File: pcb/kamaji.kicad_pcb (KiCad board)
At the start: 2 copper layers, 130 x 110 mm, 35 parts, among them J1 RJ10, J2 RJ10, J3 RJ10, J4 RJ10, J5 RJ10, Q1 TIP120, Q2 TIP120, SW1 CTRL1, SW2 CTRL2, SW3 CTRL3, U1 ATMEGA328P-PU

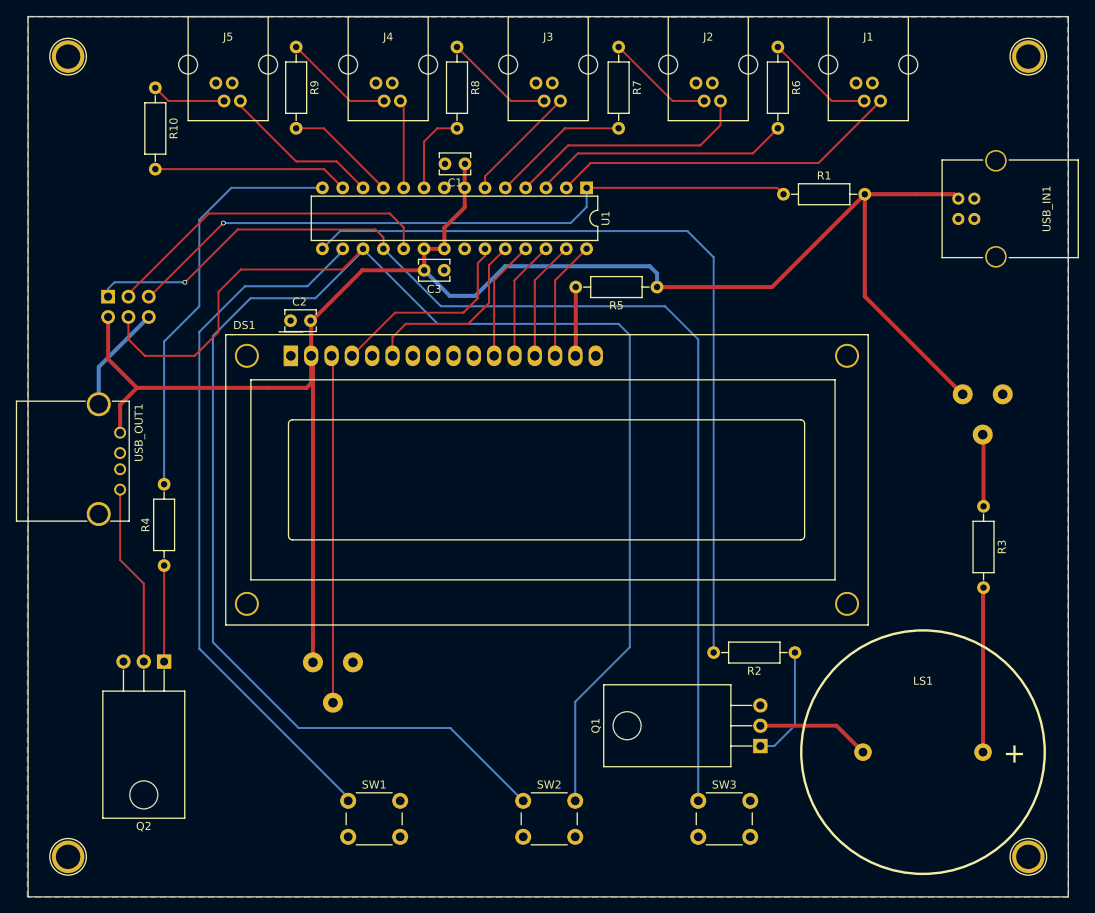
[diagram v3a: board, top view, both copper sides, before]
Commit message: change mounting hole sizes, move labels around
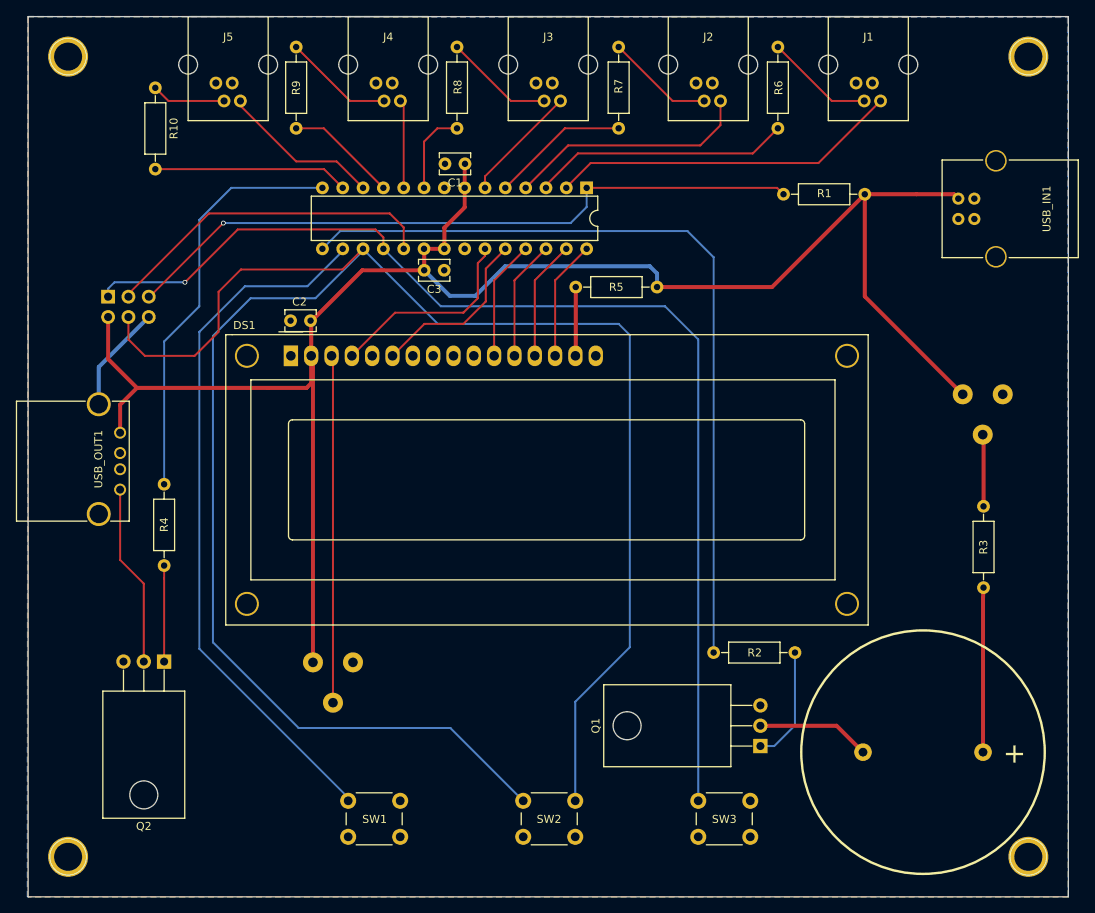
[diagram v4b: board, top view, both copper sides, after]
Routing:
- net LCD_EN: track 23.8 -> 22.1 mm
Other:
- board text added: "Ilya Strukov <iley@iley.ru>"

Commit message: miscellaneous PCB changes
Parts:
- moved USB_OUT1 2.08 mm to (113.2, 83.2)
- moved USB_IN1 1.55 mm to (214.8, 52.2)
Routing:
- net GND: track 13.7 -> 0.23 mm
- net VCC: track 225.6 -> 221.2 mm
- net Net-(Q2-Pad2): track 22.7 -> 20.8 mm
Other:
- rule trace_min: 0.2 -> 0.25
- board text added: "CONTRAST"
- board text added: "Kamaji 1.0"
- board text added: "VOLUME"
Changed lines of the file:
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@@
     (area 99.924999 29.924999 230.075001 140.075001)
     (thickness 1.6)
-    (drawings 5)
-    (tracks 192)
+    (drawings 8)
+    (tracks 185)
     (zones 0)
     (modules 35)
@@
     (zone_clearance 0.508)
     (zone_45_only no)
-    (trace_min 0.2)
+    (trace_min 0.25)
     (segment_width 0.2)
     (edge_width 0.15)
@@
     (descr "C, Disc series, Radial, pin pitch=2.50mm, , diameter*width=3.8*2.6mm^2, Capacitor, http://www.vishay.com/docs/45233/krseries.pdf")
     (tags "C Disc series Radial pin pitch 2.50mm  diameter 3.8mm width 2.6mm Capacitor")
-    (fp_text reference C1 (at 1.25 -2.36 180) (layer F.SilkS)
+    (fp_text reference C1 (at 4.3 -0.2 180) (layer F.SilkS)
       (effects (font (size 1 1) (thickness 0.15)))
     )
@@
     (descr "LCD 16x2 http://www.wincomlcd.com/pdf/WC1602A-SFYLYHTC06.pdf")
     (tags "LCD 16x2 Alphanumeric 16pin")
-    (fp_text reference DS1 (at -5.82 -3.81) (layer F.SilkS)
+    (fp_text reference DS1 (at -5.82 -3.81) (layer F.SilkS) hide
       (effects (font (size 1 1) (thickness 0.15)))
     )
@@
     (descr "Resistor, Axial_DIN0207 series, Axial, Horizontal, pin pitch=10.16mm, 0.25W = 1/4W, length*diameter=6.3*2.5mm^2, http://cdn-reichelt.de/documents/datenblatt/B400/1_4W%23YAG.pdf")
     (tags "Resistor Axial_DIN0207 series Axial Horizontal pin pitch 10.16mm 0.25W = 1/4W length 6.3mm diameter 2.5mm")
-    (fp_text reference R10 (at 5.08 -2.31 270) (layer F.SilkS)
+    (fp_text reference R10 (at 4.8 0 270) (layer F.SilkS)
       (effects (font (size 1 1) (thickness 0.15)))
     )
@@
     (descr "Potentiometer, Trimmer, RM-065")
     (tags "Potentiometer Trimmer RM-065")
-    (fp_text reference RV1 (at -2.1 2.5 270) (layer B.SilkS)
+    (fp_text reference RV1 (at 2.4 2 270) (layer B.SilkS)
       (effects (font (size 1 1) (thickness 0.15)) (justify mirror))
     )
@@
     (descr "Potentiometer, Trimmer, RM-065")
     (tags "Potentiometer Trimmer RM-065")
-    (fp_text reference RV2 (at 2.4 2 270) (layer B.SilkS)
+    (fp_text reference RV2 (at 2.4 2.3) (layer B.SilkS)
       (effects (font (size 1 1) (thickness 0.15)) (justify mirror))
     )
@@
   )
   (module Connectors:USB_B (layer F.Cu)
-    (at 216.25 52.75)
+    (at 214.8 52.2)
     (descr "USB B connector")
     (tags "USB_B USB_DEV")
@@
   )
   (module Connectors:USB_A (layer F.Cu)
-    (at 111.5 82 270)
+    (at 113.2 83.2 270)
     (descr "USB A connector")
     (tags "USB USB_A")
@@
       (effects (font (size 1 1) (thickness 0.15)) (justify mirror))
     )
-    (fp_text value ICSP (at 3 -5) (layer B.Fab)
+    (fp_text value ICSP (at 3 -5) (layer B.SilkS)
       (effects (font (size 1 1) (thickness 0.15)) (justify mirror))
     )
@@
     (pad 1 thru_hole circle (at 0 0) (size 5 5) (drill 3.5) (layers *.Cu *.Mask))
   )
-  (gr_text "Ilya Strukov <iley@iley.ru>" (at 104.8 113.1 90) (layer F.Mask)
+  (gr_text VOLUME (at 219.4 85.5) (layer B.SilkS)
+    (effects (font (size 1 1) (thickness 0.15)) (justify mirror))
+  )
+  (gr_text CONTRAST (at 138.2 119.1) (layer B.SilkS)
+    (effects (font (size 1 1) (thickness 0.15)) (justify mirror))
+  )
+  (gr_text "Kamaji 1.0" (at 105 112.7 90) (layer F.SilkS)
+    (effects (font (size 1.5 1.5) (thickness 0.3)))
+  )
+  (gr_text "Ilya Strukov <iley@iley.ru>" (at 105 56.9 90) (layer F.SilkS)
     (effects (font (size 1.5 1.5) (thickness 0.3)))
   )
@@
   (gr_line (start 100 140) (end 100 30) (angle 90) (layer Edge.Cuts) (width 0.15))
   (gr_line (start 230 140) (end 100 140) (angle 90) (layer Edge.Cuts) (width 0.15))
+  (segment (start 113.2 83.2) (end 135.6 83.2) (width 0.5) (layer F.Cu) (net 1) (status 400000))
+  (segment (start 135.6 83.2) (end 135.6 83.1) (width 0.5) (layer F.Cu) (net 1))
+  (segment (start 113.2 83.2) (end 113.2 77.1) (width 0.5) (layer F.Cu) (net 1) (status 400000))
+  (segment (start 110 73.9) (end 110 67.54) (width 0.5) (layer F.Cu) (net 1) (status 800000))
+  (segment (start 113.2 77.1) (end 110 73.9) (width 0.5) (layer F.Cu) (net 1))
+  (segment (start 204.56 52.2) (end 214.8 52.2) (width 0.5) (layer F.Cu) (net 1))
   (segment (start 178.6 63.8) (end 178.6 62.1) (width 0.5) (layer B.Cu) (net 1))
   (segment (start 152.7 64.9) (end 149.5 61.7) (width 0.5) (layer B.Cu) (net 1))
@@
   (segment (start 177.7 61.2) (end 159.6 61.2) (width 0.5) (layer B.Cu) (net 1))
   (segment (start 178.6 62.1) (end 177.7 61.2) (width 0.5) (layer B.Cu) (net 1))
-  (segment (start 135.6 110.7) (end 135.6 72.608) (width 0.5) (layer F.Cu) (net 1))
+  (segment (start 135.6 110.7) (end 135.6 83.1) (width 0.5) (layer F.Cu) (net 1))
+  (segment (start 135.6 83.1) (end 135.6 72.608) (width 0.5) (layer F.Cu) (net 1))
   (segment (start 135.6 72.608) (end 135.382 72.39) (width 0.5) (layer F.Cu) (net 1))
   (segment (start 178.6 63.8) (end 192.96 63.8) (width 0.5) (layer F.Cu) (net 1))
@@
   (segment (start 154.56 48.44) (end 154.6 48.4) (width 0.5) (layer F.Cu) (net 1))
   (segment (start 151.9 59.14) (end 152.02 59.02) (width 0.5) (layer F.Cu) (net 1))
-  (segment (start 204.56 52.2) (end 211 52.2) (width 0.5) (layer F.Cu) (net 1))
-  (segment (start 211 52.2) (end 215.7 52.2) (width 0.5) (layer F.Cu) (net 1))
-  (segment (start 215.7 52.2) (end 216.25 52.75) (width 0.5) (layer F.Cu) (net 1) (status 20))
-  (segment (start 111.5 82) (end 111.5 78.5) (width 0.5) (layer F.Cu) (net 1))
-  (segment (start 111.5 78.5) (end 113.6 76.4) (width 0.5) (layer F.Cu) (net 1))
   (segment (start 149.48 59.02) (end 152.02 59.02) (width 0.5) (layer F.Cu) (net 1) (status 30))
-  (segment (start 110 67.54) (end 110 72.8) (width 0.5) (layer F.Cu) (net 1))
-  (segment (start 135.382 75.818) (end 135.382 72.39) (width 0.5) (layer F.Cu) (net 1))
-  (segment (start 134.8 76.4) (end 135.382 75.818) (width 0.5) (layer F.Cu) (net 1))
-  (segment (start 113.6 76.4) (end 130 76.4) (width 0.5) (layer F.Cu) (net 1))
-  (segment (start 130 76.4) (end 134.8 76.4) (width 0.5) (layer F.Cu) (net 1))
-  (segment (start 110 72.8) (end 113.6 76.4) (width 0.5) (layer F.Cu) (net 1))
   (segment (start 154.61 48.41) (end 154.6 48.4) (width 0.5) (layer F.Cu) (net 1) (status 30))
-  (segment (start 108.83 78.44) (end 108.83 73.79) (width 0.5) (layer B.Cu) (net 2))
-  (segment (start 108.83 73.79) (end 115.08 67.54) (width 0.5) (layer B.Cu) (net 2))
   (segment (start 154.4 59.18) (end 154.56 59.02) (width 0.5) (layer F.Cu) (net 2))
   (segment (start 138.1 115.74) (end 138.1 72.568) (width 0.25) (layer F.Cu) (net 3))
@@
   (segment (start 154.4 67) (end 145.852 67) (width 0.25) (layer F.Cu) (net 4))
   (segment (start 145.852 67) (end 140.462 72.39) (width 0.25) (layer F.Cu) (net 4))
-  (segment (start 159.64 59.02) (end 159.64 59.06) (width 0.25) (layer F.Cu) (net 5) (status C00000))
-  (segment (start 159.64 59.06) (end 157.2 61.5) (width 0.25) (layer F.Cu) (net 5) (status 400000))
+  (segment (start 159.64 59.02) (end 159.64 59.06) (width 0.25) (layer F.Cu) (net 5))
+  (segment (start 159.64 59.06) (end 157.2 61.5) (width 0.25) (layer F.Cu) (net 5))
   (segment (start 157.2 61.5) (end 157.2 65.6) (width 0.25) (layer F.Cu) (net 5))
   (segment (start 157.2 65.6) (end 154.4 68.4) (width 0.25) (layer F.Cu) (net 5))
   (segment (start 154.4 68.4) (end 149.532 68.4) (width 0.25) (layer F.Cu) (net 5))
-  (segment (start 149.532 68.4) (end 145.542 72.39) (width 0.25) (layer F.Cu) (net 5) (status 800000))
+  (segment (start 149.532 68.4) (end 145.542 72.39) (width 0.25) (layer F.Cu) (net 5))
   (segment (start 158.242 72.39) (end 158.242 62.958) (width 0.25) (layer F.Cu) (net 10))
   (segment (start 158.242 62.958) (end 162.18 59.02) (width 0.25) (layer F.Cu) (net 10))
@@
   (segment (start 117 110.6) (end 117 100.2) (width 0.25) (layer F.Cu) (net 29))
   (segment (start 117 100.2) (end 117 98.6) (width 0.25) (layer F.Cu) (net 29) (status 20))
-  (segment (start 111.5 89.11) (end 111.5 97.9) (width 0.25) (layer F.Cu) (net 30))
-  (segment (start 111.5 97.9) (end 114.46 100.86) (width 0.25) (layer F.Cu) (net 30))
-  (segment (start 114.46 100.86) (end 114.46 110.6) (width 0.25) (layer F.Cu) (net 30))
+  (segment (start 114.46 110.6) (end 114.46 91.57) (width 0.25) (layer F.Cu) (net 30) (status 400000))
+  (segment (start 114.46 91.57) (end 113.2 90.31) (width 0.25) (layer F.Cu) (net 30) (status 800000))
   (segment (start 185.674 109.474) (end 185.674 60.074) (width 0.25) (layer B.Cu) (net 31))
   (segment (start 185.674 60.074) (end 182.4 56.8) (width 0.25) (layer B.Cu) (net 31))

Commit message: final touches to the PCB design
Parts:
- moved R1 19.9 mm to (174.5, 51.4)
- moved USB_IN1 0.92 mm to (214.6, 51.3)
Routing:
- net RST: track 86.8 -> 66.5 mm
- net VCC: track 221.2 -> 224.5 mm
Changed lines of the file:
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@@
     (links 87)
     (no_connects 2)
-    (area 99.924999 29.924999 230.075001 140.075001)
+    (area 99.774999 29.55 230.275001 140.075001)
     (thickness 1.6)
     (drawings 8)
-    (tracks 185)
+    (tracks 187)
     (zones 0)
     (modules 35)
@@
   )
   (module Resistors_THT:R_Axial_DIN0207_L6.3mm_D2.5mm_P10.16mm_Horizontal (layer F.Cu)
-    (at 194.4 52.2)
+    (at 174.5 51.4)
     (descr "Resistor, Axial_DIN0207 series, Axial, Horizontal, pin pitch=10.16mm, 0.25W = 1/4W, length*diameter=6.3*2.5mm^2, http://cdn-reichelt.de/documents/datenblatt/B400/1_4W%23YAG.pdf")
     (tags "Resistor Axial_DIN0207 series Axial Horizontal pin pitch 10.16mm 0.25W = 1/4W length 6.3mm diameter 2.5mm")
@@
   )
   (module Connectors:USB_B (layer F.Cu)
-    (at 214.8 52.2)
+    (at 214.6 51.3)
     (descr "USB B connector")
     (tags "USB_B USB_DEV")
@@
   (gr_line (start 100 140) (end 100 30) (angle 90) (layer Edge.Cuts) (width 0.15))
   (gr_line (start 230 140) (end 100 140) (angle 90) (layer Edge.Cuts) (width 0.15))
-  (segment (start 113.2 83.2) (end 135.6 83.2) (width 0.5) (layer F.Cu) (net 1) (status 400000))
+  (segment (start 194.35 52.25) (end 194.4 52.2) (width 0.25) (layer F.Cu) (net 0))
+  (segment (start 194.35 52.25) (end 194.4 52.2) (width 0.25) (layer F.Cu) (net 0))
+  (segment (start 214.6 51.3) (end 214.5 51.3) (width 0.5) (layer F.Cu) (net 1) (status C00000))
+  (segment (start 214.5 51.3) (end 211.4 54.4) (width 0.5) (layer F.Cu) (net 1) (status 400000))
+  (segment (start 211.4 71.8) (end 216.8 77.2) (width 0.5) (layer F.Cu) (net 1) (status 800000))
+  (segment (start 211.4 54.4) (end 211.4 71.8) (width 0.5) (layer F.Cu) (net 1))
+  (segment (start 178.6 63.8) (end 178.6 57.46) (width 0.5) (layer F.Cu) (net 1) (status 400000))
+  (segment (start 178.6 57.46) (end 184.66 51.4) (width 0.5) (layer F.Cu) (net 1) (status 800000))
+  (segment (start 184.66 51.4) (end 214.5 51.4) (width 0.5) (layer F.Cu) (net 1) (status C00000))
+  (segment (start 214.5 51.4) (end 214.6 51.3) (width 0.5) (layer F.Cu) (net 1) (status C00000))
+  (segment (start 113.2 83.2) (end 135.6 83.2) (width 0.5) (layer F.Cu) (net 1))
   (segment (start 135.6 83.2) (end 135.6 83.1) (width 0.5) (layer F.Cu) (net 1))
-  (segment (start 113.2 83.2) (end 113.2 77.1) (width 0.5) (layer F.Cu) (net 1) (status 400000))
-  (segment (start 110 73.9) (end 110 67.54) (width 0.5) (layer F.Cu) (net 1) (status 800000))
+  (segment (start 113.2 83.2) (end 113.2 77.1) (width 0.5) (layer F.Cu) (net 1))
+  (segment (start 110 73.9) (end 110 67.54) (width 0.5) (layer F.Cu) (net 1))
   (segment (start 113.2 77.1) (end 110 73.9) (width 0.5) (layer F.Cu) (net 1))
-  (segment (start 204.56 52.2) (end 214.8 52.2) (width 0.5) (layer F.Cu) (net 1))
   (segment (start 178.6 63.8) (end 178.6 62.1) (width 0.5) (layer B.Cu) (net 1))
   (segment (start 152.7 64.9) (end 149.5 61.7) (width 0.5) (layer B.Cu) (net 1))
@@
   (segment (start 135.6 83.1) (end 135.6 72.608) (width 0.5) (layer F.Cu) (net 1))
   (segment (start 135.6 72.608) (end 135.382 72.39) (width 0.5) (layer F.Cu) (net 1))
-  (segment (start 178.6 63.8) (end 192.96 63.8) (width 0.5) (layer F.Cu) (net 1))
-  (segment (start 192.96 63.8) (end 204.56 52.2) (width 0.5) (layer F.Cu) (net 1))
-  (segment (start 204.56 52.2) (end 204.56 64.96) (width 0.5) (layer F.Cu) (net 1))
-  (segment (start 204.56 64.96) (end 216.8 77.2) (width 0.5) (layer F.Cu) (net 1))
   (segment (start 135.382 72.39) (end 135.382 68.082) (width 0.5) (layer F.Cu) (net 1))
   (segment (start 135.382 68.082) (end 141.764 61.7) (width 0.5) (layer F.Cu) (net 1))
@@
   (segment (start 126.6 61.6) (end 139.28 61.6) (width 0.25) (layer F.Cu) (net 24))
   (segment (start 139.28 61.6) (end 141.86 59.02) (width 0.25) (layer F.Cu) (net 24))
+  (segment (start 169.8 51.4) (end 174.5 51.4) (width 0.25) (layer F.Cu) (net 25))
   (segment (start 169.8 51.4) (end 169.8 53.8) (width 0.25) (layer B.Cu) (net 25))
   (segment (start 169.8 53.8) (end 167.8 55.8) (width 0.25) (layer B.Cu) (net 25))
@@
   (segment (start 124.4 55.8) (end 115.2 65) (width 0.25) (layer F.Cu) (net 25))
   (segment (start 115.2 65) (end 115.08 65) (width 0.25) (layer F.Cu) (net 25))
-  (segment (start 169.8 51.4) (end 193.6 51.4) (width 0.25) (layer F.Cu) (net 25))
-  (segment (start 193.6 51.4) (end 194.4 52.2) (width 0.25) (layer F.Cu) (net 25))
-  (segment (start 194.35 52.25) (end 194.4 52.2) (width 0.25) (layer F.Cu) (net 25))
-  (segment (start 194.35 52.25) (end 194.4 52.2) (width 0.25) (layer F.Cu) (net 25))
   (segment (start 219.336 121.92) (end 219.336 102.696) (width 0.5) (layer F.Cu) (net 26))
   (segment (start 219.336 102.696) (end 219.4 101.36) (width 0.5) (layer F.Cu) (net 26) (status 20))
@@
   (segment (start 117 110.6) (end 117 100.2) (width 0.25) (layer F.Cu) (net 29))
   (segment (start 117 100.2) (end 117 98.6) (width 0.25) (layer F.Cu) (net 29) (status 20))
-  (segment (start 114.46 110.6) (end 114.46 91.57) (width 0.25) (layer F.Cu) (net 30) (status 400000))
-  (segment (start 114.46 91.57) (end 113.2 90.31) (width 0.25) (layer F.Cu) (net 30) (status 800000))
+  (segment (start 114.46 110.6) (end 114.46 91.57) (width 0.25) (layer F.Cu) (net 30))
+  (segment (start 114.46 91.57) (end 113.2 90.31) (width 0.25) (layer F.Cu) (net 30))
   (segment (start 185.674 109.474) (end 185.674 60.074) (width 0.25) (layer B.Cu) (net 31))
   (segment (start 185.674 60.074) (end 182.4 56.8) (width 0.25) (layer B.Cu) (net 31))
